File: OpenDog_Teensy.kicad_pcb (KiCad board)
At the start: 2 copper layers, 61.6 x 96 mm, 58 parts, among them J1 NRF, J10 UART5, J11 UART6, J12 CAN1, J13 CAN2, J14 EXP, J15 Power, J2 TOF1, J3 TOF2, J4 IMU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

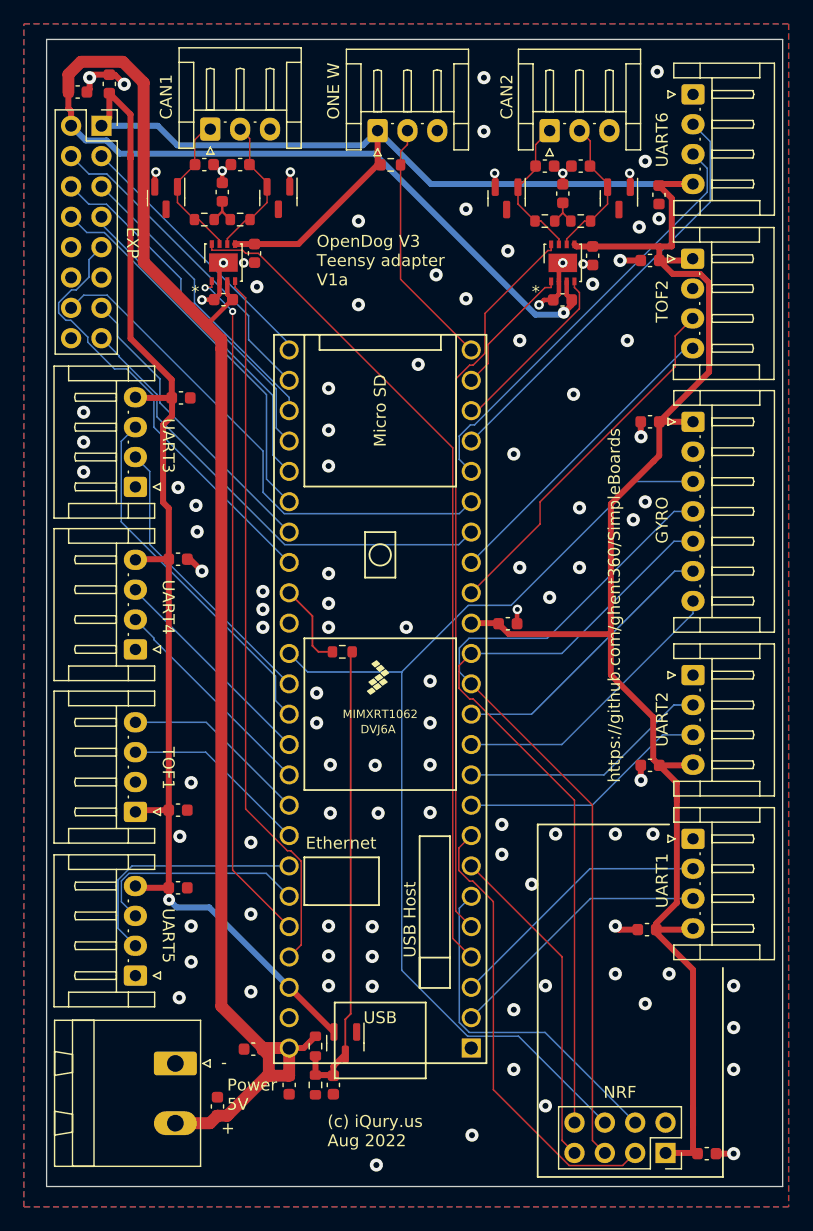
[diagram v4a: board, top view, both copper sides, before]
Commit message: Update OpenDog board part numbers. Small routing changes.
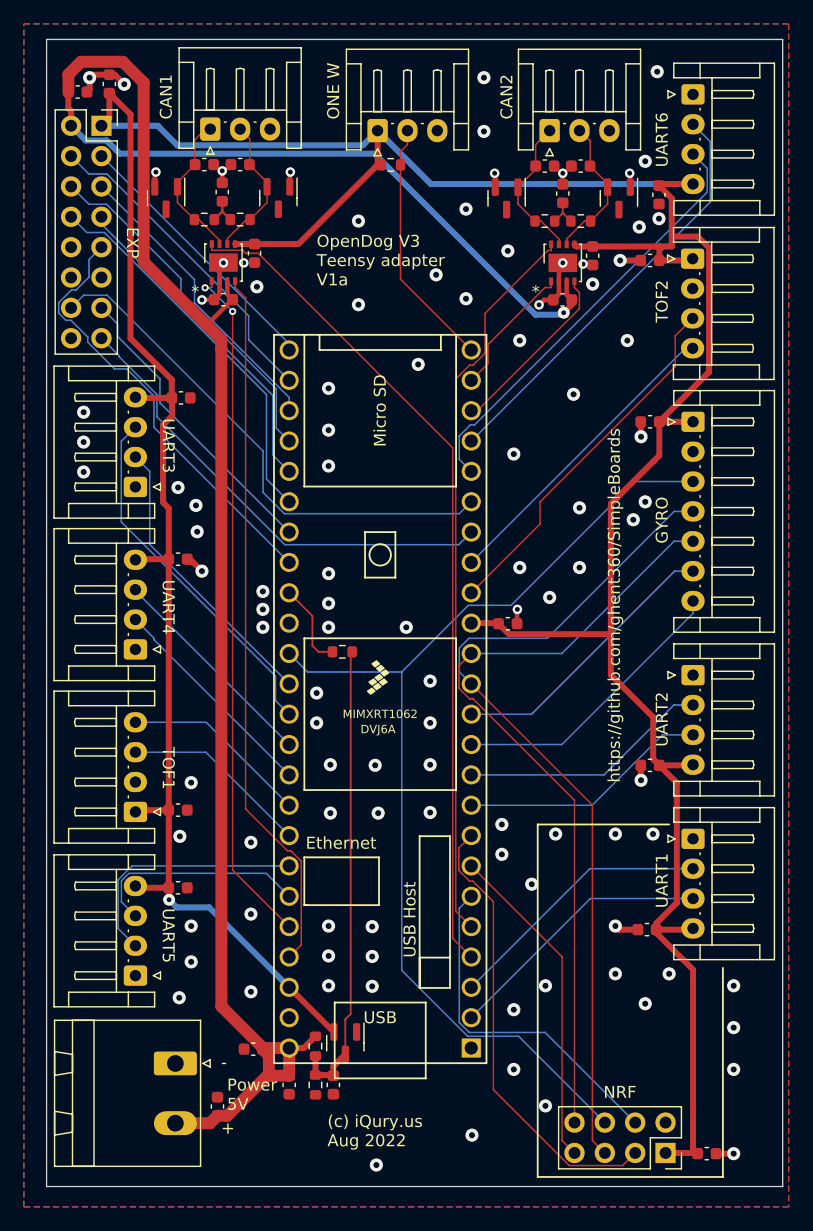
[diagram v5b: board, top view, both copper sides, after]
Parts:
- R1, R2, R3, R4: value 60 -> 60.4
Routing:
- net /3.3V: track 306.4 -> 305.0 mm
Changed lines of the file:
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@@
     (descr "Resistor SMD 0603 (1608 Metric), square (rectangular) end terminal, IPC_7351 nominal, (Body size source: IPC-SM-782 page 72, https://www.pcb-3d.com/wordpress/wp-content/uploads/ipc-sm-782a_amendment_1_and_2.pdf), generated with kicad-footprint-generator")
     (tags "resistor")
+    (property "JLC Part #" "C23090")
     (property "Sheetfile" "File: OpenDog_Teensy.kicad_sch")
     (property "Sheetname" "")
@@
         (effects (font (size 1 1) (thickness 0.15)))
     )
-    (fp_text value "60" (at 0 1.43) (layer "F.Fab")
+    (fp_text value "60.4" (at 0 1.43) (layer "F.Fab")
         (effects (font (size 1 1) (thickness 0.15)))
     )
@@
     (descr "Resistor SMD 0603 (1608 Metric), square (rectangular) end terminal, IPC_7351 nominal, (Body size source: IPC-SM-782 page 72, https://www.pcb-3d.com/wordpress/wp-content/uploads/ipc-sm-782a_amendment_1_and_2.pdf), generated with kicad-footprint-generator")
     (tags "resistor")
+    (property "JLC Part #" "C23090")
     (property "Sheetfile" "File: OpenDog_Teensy.kicad_sch")
     (property "Sheetname" "")
@@
         (effects (font (size 1 1) (thickness 0.15)))
     )
-    (fp_text value "60" (at 0 1.43) (layer "F.Fab")
+    (fp_text value "60.4" (at 0 1.43) (layer "F.Fab")
         (effects (font (size 1 1) (thickness 0.15)))
     )
@@
     (descr "Generic Phoenix Contact connector footprint for: MSTBA_2,5/2-G; number of pins: 02; pin pitch: 5.00mm; Angled || order number: 1757475 12A || order number: 1923759 16A (HC)")
     (tags "phoenix_contact connector MSTBA_01x02_G_5.00mm")
-    (property "JLC Part #" "C8439")
+    (property "JLC Part #" "C8404")
     (property "Sheetfile" "File: OpenDog_Teensy.kicad_sch")
     (property "Sheetname" "")
@@
     (descr "Resistor SMD 0603 (1608 Metric), square (rectangular) end terminal, IPC_7351 nominal, (Body size source: IPC-SM-782 page 72, https://www.pcb-3d.com/wordpress/wp-content/uploads/ipc-sm-782a_amendment_1_and_2.pdf), generated with kicad-footprint-generator")
     (tags "resistor")
+    (property "JLC Part #" "C23090")
     (property "Sheetfile" "File: OpenDog_Teensy.kicad_sch")
     (property "Sheetname" "")
@@
         (effects (font (size 1 1) (thickness 0.15)))
     )
-    (fp_text value "60" (at 0 1.43) (layer "F.Fab")
+    (fp_text value "60.4" (at 0 1.43) (layer "F.Fab")
         (effects (font (size 1 1) (thickness 0.15)))
     )
@@
     (descr "Resistor SMD 0603 (1608 Metric), square (rectangular) end terminal, IPC_7351 nominal, (Body size source: IPC-SM-782 page 72, https://www.pcb-3d.com/wordpress/wp-content/uploads/ipc-sm-782a_amendment_1_and_2.pdf), generated with kicad-footprint-generator")
     (tags "resistor")
+    (property "JLC Part #" "C23090")
     (property "Sheetfile" "File: OpenDog_Teensy.kicad_sch")
     (property "Sheetname" "")
@@
         (effects (font (size 1 1) (thickness 0.15)))
     )
-    (fp_text value "60" (at 0 1.43) (layer "F.Fab")
+    (fp_text value "60.4" (at 0 1.43) (layer "F.Fab")
         (effects (font (size 1 1) (thickness 0.15)))
     )
@@
   (segment (start 79.425 72.5) (end 78.923 72.5) (width 0.127) (layer "F.Cu") (net 8))
   (segment (start 79.375 67.9) (end 80.85 69.375) (width 0.127) (layer "F.Cu") (net 8))
-  (segment (start 40.923499 67.276501) (end 40.923499 66.958499) (width 0.5) (layer "F.Cu") (net 9))
+  (segment (start 86.225 70.6) (end 86.225 73.975) (width 0.5) (layer "F.Cu") (net 9))
+  (segment (start 86.4 73.8) (end 86.225 73.975) (width 0.5) (layer "F.Cu") (net 9))
   (segment (start 44.15 128.325) (end 44.125 128.3) (width 0.5) (layer "F.Cu") (net 9))
   (segment (start 85.225 74.625) (end 79.6 74.625) (width 0.5) (layer "F.Cu") (net 9))
-  (segment (start 88.60074 76.923) (end 89.3436 77.66586) (width 0.5) (layer "F.Cu") (net 9))
   (segment (start 81.1255 107.0707) (end 72.5957 107.0707) (width 0.5) (layer "F.Cu") (net 9))
   (segment (start 44.4 88.8) (end 44.4 87.325) (width 0.5) (layer "F.Cu") (net 9))
@@
   (segment (start 43.65 96.05) (end 43.65 89.55) (width 0.5) (layer "F.Cu") (net 9))
   (segment (start 40.923499 63.573499) (end 39.15 61.8) (width 0.5) (layer "F.Cu") (net 9))
-  (segment (start 85.175 75.8) (end 87.8175 75.8) (width 0.5) (layer "F.Cu") (net 9))
   (segment (start 44.125 128.3) (end 41.4825 128.3) (width 0.5) (layer "F.Cu") (net 9))
-  (segment (start 86.6466 120.5807) (end 86.6466 121.0534) (width 0.5) (layer "F.Cu") (net 9))
-  (segment (start 88 146.7) (end 88 148.19) (width 0.5) (layer "F.Cu") (net 9))
   (segment (start 44.375 85.775) (end 40.923499 82.323499) (width 0.5) (layer "F.Cu") (net 9))
   (segment (start 85.7 150.49) (end 88.315 150.49) (width 0.5) (layer "F.Cu") (net 9))
   (segment (start 44.125 100.8) (end 44.125 96.525) (width 0.5) (layer "F.Cu") (net 9))
   (segment (start 84.925 131.275) (end 84.925 131.8) (width 0.5) (layer "F.Cu") (net 9))
-  (segment (start 88 75.6175) (end 87.9675 75.65) (width 1) (layer "F.Cu") (net 9))
   (segment (start 84.6696 114.0304) (end 84.6696 117.5446) (width 0.5) (layer "F.Cu") (net 9))
   (segment (start 44.125 100.8) (end 41.3825 100.8) (width 0.5) (layer "F.Cu") (net 9))
@@
   (segment (start 41.4825 121.8) (end 41.3325 121.95) (width 0.5) (layer "F.Cu") (net 9))
   (segment (start 81.1255 96.1745) (end 81.1255 107.0707) (width 0.5) (layer "F.Cu") (net 9))
+  (segment (start 87.8175 75.8) (end 87.9675 75.65) (width 0.5) (layer "F.Cu") (net 9))
   (segment (start 85.275 69.4) (end 85.15 69.525) (width 0.5) (layer "F.Cu") (net 9))
   (segment (start 81.1255 110.4863) (end 84.6696 114.0304) (width 0.5) (layer "F.Cu") (net 9))
@@
   (segment (start 44.125 121.8) (end 44.125 100.8) (width 0.5) (layer "F.Cu") (net 9))
   (segment (start 85.15 69.525) (end 86.225 70.6) (width 0.5) (layer "F.Cu") (net 9))
+  (segment (start 86.225 73.975) (end 86.225 74.625) (width 0.5) (layer "F.Cu") (net 9))
   (segment (start 86.6466 121.0534) (end 86.6466 119.5216) (width 0.5) (layer "F.Cu") (net 9))
   (segment (start 88 135.15) (end 88 146.7) (width 0.5) (layer "F.Cu") (net 9))
   (segment (start 44.4 87.325) (end 44.375 87.3) (width 0.5) (layer "F.Cu") (net 9))
-  (segment (start 87.8175 75.8) (end 87.9675 75.65) (width 0.5) (layer "F.Cu") (net 9))
   (segment (start 51.3 74.425) (end 49.675 74.425) (width 0.5) (layer "F.Cu") (net 9))
+  (segment (start 89.3436 78.8564) (end 89.3436 74.7436) (width 0.5) (layer "F.Cu") (net 9))
+  (segment (start 85.175 75.8) (end 87.8175 75.8) (width 0.5) (layer "F.Cu") (net 9))
   (segment (start 88 150.175) (end 88.375 150.55) (width 0.5) (layer "F.Cu") (net 9))
   (segment (start 57.95 140.3625) (end 57.9325 140.3625) (width 0.5) (layer "F.Cu") (net 9))
-  (segment (start 86.298 76.923) (end 88.60074 76.923) (width 0.5) (layer "F.Cu") (net 9))
   (segment (start 44.125 121.8) (end 41.4825 121.8) (width 0.5) (layer "F.Cu") (net 9))
   (segment (start 85.175 89.3) (end 88 89.3) (width 0.5) (layer "F.Cu") (net 9))
   (segment (start 86.6466 119.5216) (end 85.175 118.05) (width 0.5) (layer "F.Cu") (net 9))
   (segment (start 89.3436 85.1314) (end 85.175 89.3) (width 0.5) (layer "F.Cu") (net 9))
+  (segment (start 89.3436 78.8564) (end 89.3436 85.1314) (width 0.5) (layer "F.Cu") (net 9))
   (segment (start 51.3 74.425) (end 54.975 74.425) (width 0.5) (layer "F.Cu") (net 9))
   (segment (start 39.15 61.8) (end 39.15 63.865) (width 0.5) (layer "F.Cu") (net 9))
@@
   (segment (start 86.6466 121.0534) (end 86.6466 129.5534) (width 0.5) (layer "F.Cu") (net 9))
   (segment (start 39.15 63.865) (end 38.49 64.525) (width 0.5) (layer "F.Cu") (net 9))
+  (segment (start 89.3436 74.7436) (end 88.4 73.8) (width 0.5) (layer "F.Cu") (net 9))
   (segment (start 57.9325 140.3625) (end 54.2 136.63) (width 0.5) (layer "F.Cu") (net 9))
   (segment (start 88 146.7) (end 88 150.175) (width 0.5) (layer "F.Cu") (net 9))
@@
   (segment (start 85.175 92.125) (end 85.175 89.3) (width 0.5) (layer "F.Cu") (net 9))
   (segment (start 54.975 74.425) (end 61.6 67.8) (width 0.5) (layer "F.Cu") (net 9))
-  (segment (start 86.225 70.6) (end 86.225 74.625) (width 0.5) (layer "F.Cu") (net 9))
   (segment (start 69.44 106.15) (end 71.675 106.15) (width 0.5) (layer "F.Cu") (net 9))
   (segment (start 85.175 74.675) (end 85.225 74.625) (width 0.5) (layer "F.Cu") (net 9))
   (segment (start 44.375 87.3) (end 41.3825 87.3) (width 0.5) (layer "F.Cu") (net 9))
   (segment (start 84.925 131.8) (end 84.925 132.075) (width 0.5) (layer "F.Cu") (net 9))
-  (segment (start 89.3436 77.66586) (end 89.3436 85.1314) (width 0.5) (layer "F.Cu") (net 9))
   (segment (start 44.375 87.3) (end 44.375 85.775) (width 0.5) (layer "F.Cu") (net 9))
   (segment (start 41.3825 87.3) (end 41.3325 87.25) (width 0.5) (layer "F.Cu") (net 9))
   (segment (start 87.9 131.8) (end 88 131.7) (width 0.5) (layer "F.Cu") (net 9))
-  (segment (start 88 117.3608) (end 88 118) (width 0.5) (layer "F.Cu") (net 9))
   (segment (start 61.6 67.8) (end 61.6 64.9325) (width 0.5) (layer "F.Cu") (net 9))
   (segment (start 85.175 75.8) (end 85.175 74.675) (width 0.5) (layer "F.Cu") (net 9))
+  (segment (start 88.4 73.8) (end 86.4 73.8) (width 0.5) (layer "F.Cu") (net 9))
   (segment (start 61.6 67.8) (end 61.875 67.8) (width 0.5) (layer "F.Cu") (net 9))
   (segment (start 84.6696 117.5446) (end 85.175 118.05) (width 0.5) (layer "F.Cu") (net 9))
   (segment (start 44.125 128.3) (end 44.125 121.8) (width 0.5) (layer "F.Cu") (net 9))
   (segment (start 85.175 118.05) (end 87.95 118.05) (width 0.5) (layer "F.Cu") (net 9))
-  (segment (start 85.175 75.8) (end 86.298 76.923) (width 0.5) (layer "F.Cu") (net 9))
   (via (at 44.15 129.3) (size 1) (drill 0.4) (layers "F.Cu" "B.Cu") (net 9))
   (segment (start 44.79 129.94) (end 44.15 129.3) (width 0.5) (layer "B.Cu") (net 9))

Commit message: Added I2C pullups to the OpenDog board.
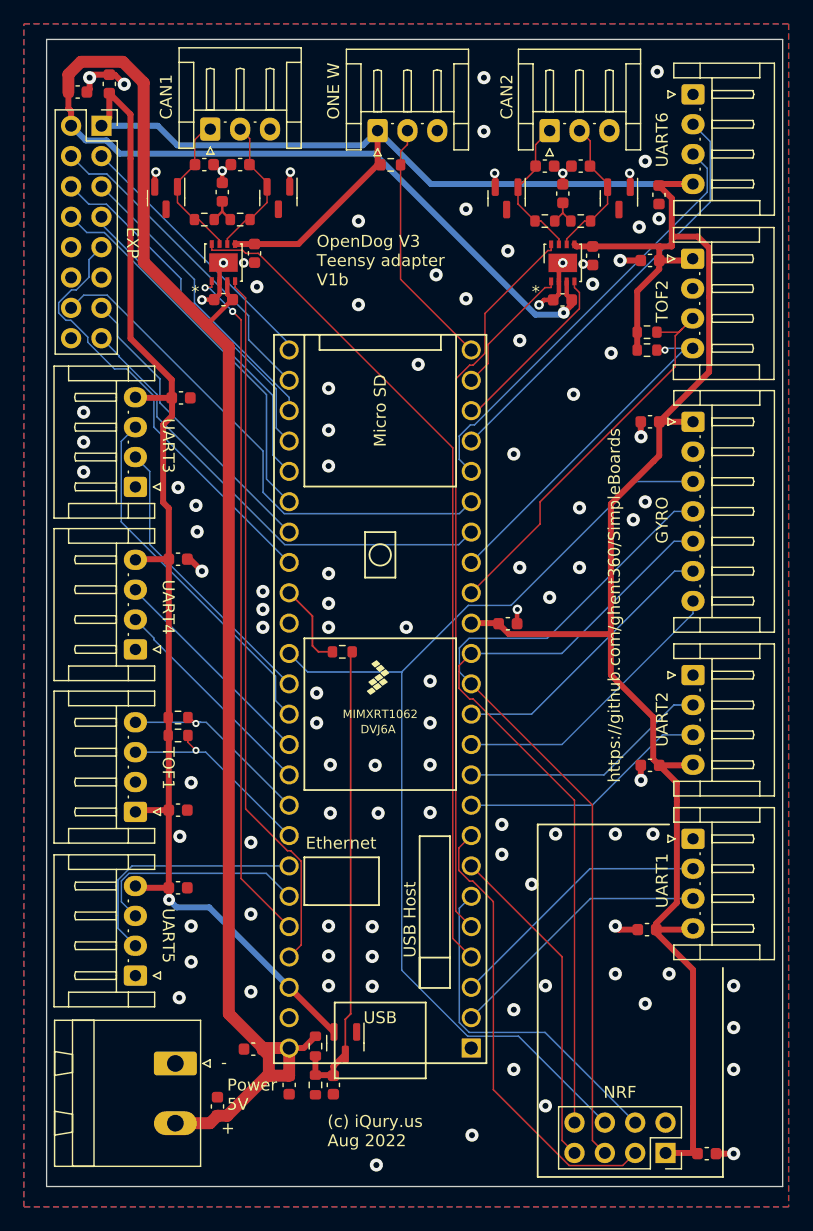
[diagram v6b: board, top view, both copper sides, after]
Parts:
- added R10: 1k, Resistor_SMD:R_0603_1608Metric, F.Cu at (44.9, 114.0)
- added R11: 1k, Resistor_SMD:R_0603_1608Metric, F.Cu at (84.2, 83.3)
- added R12: 1k, Resistor_SMD:R_0603_1608Metric, F.Cu at (84.2, 81.8)
- added R9: 1k, Resistor_SMD:R_0603_1608Metric, F.Cu at (44.9, 115.5)
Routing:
- net /3.3V: track 305.0 -> 313.3 mm
- net /SDA2: track 26.0 -> 29.0 mm, vias 0 -> 1
- net /SCL2: track 30.6 -> 32.9 mm
- net /SCL1: track 15.8 -> 17.5 mm, vias 0 -> 1
- net /SDA1: track 15.7 -> 17.1 mm, vias 0 -> 1
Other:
- board text added: "OpenDog V3 Teensy adapter V1b"
- board text removed: "OpenDog V3 Teensy adapter V1a"

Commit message: Fixed NRF connector pinout.
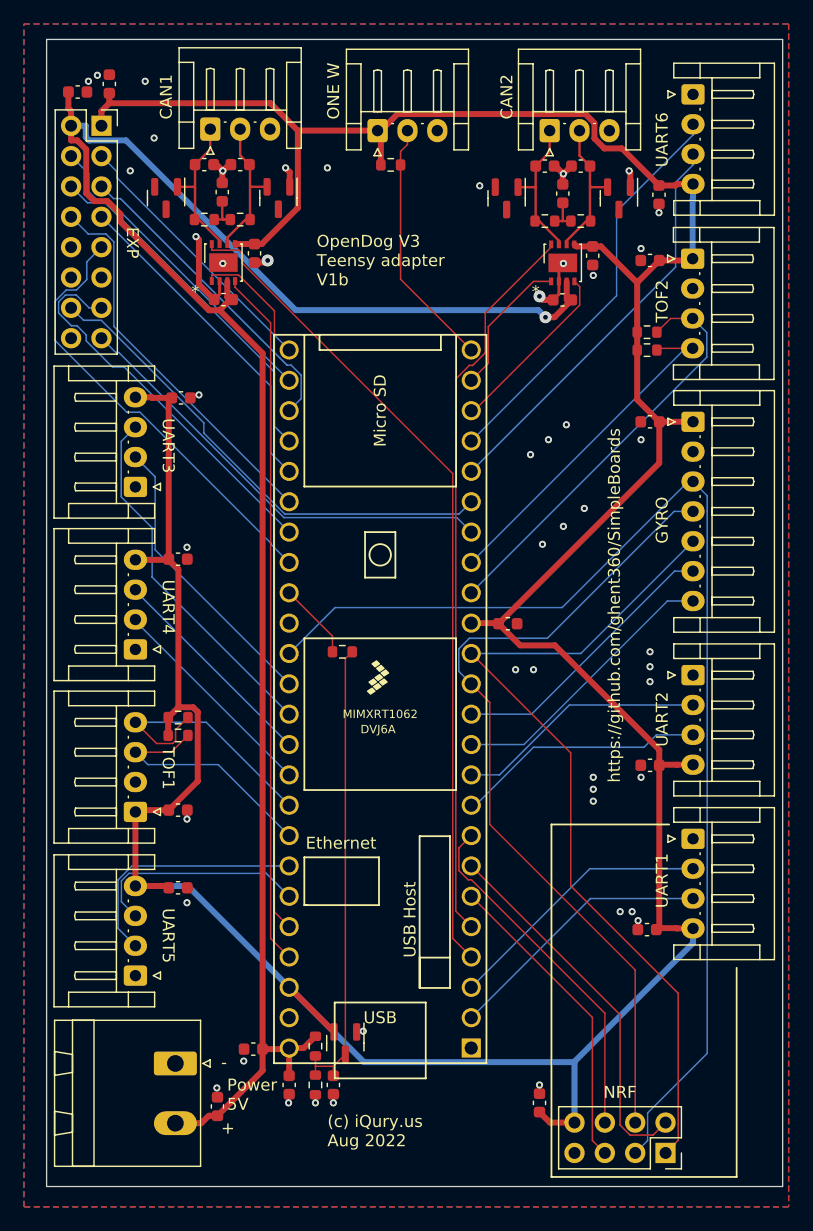
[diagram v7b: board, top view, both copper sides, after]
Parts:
- moved C24 14.6 mm to (75.2, 146.3), turned to 90 degrees
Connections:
- J1 pad 1: /3.3V -> /MISO
- J1 pad 2: GND -> /NRF_IRQ
- J1 pad 3: /~{CS_NRF} -> /SCK
- J1 pad 4: /NRF_ENA -> /MOSI
- J1 pad 5: /MOSI -> /NRF_ENA
- J1 pad 6: /SCK -> /~{CS_NRF}
- J1 pad 7: /NRF_IRQ -> GND
- J1 pad 8: /MISO -> /3.3V
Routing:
- net /3.3V: track 313.3 -> 299.0 mm, vias 1 -> 0
- net /VIn: track 173.6 -> 160.7 mm
- net /SCK: track 88.3 -> 98.9 mm
- net GND: track 31.2 -> 22.4 mm, vias 104 -> 49
- net /~{CS_NRF}: track 38.0 -> 29.7 mm
- net /MISO1: track 25.3 -> 32.4 mm
- net /MISO: track 66.3 -> 71.9 mm
- net /SDA1: track 17.1 -> 22.3 mm, vias 1 -> 0
- net /NRF_IRQ: track 27.6 -> 31.4 mm
- net /SCL1: track 17.5 -> 20.7 mm, vias 1 -> 0
- net /NRF_ENA: track 29.2 -> 26.1 mm
- net /SCK1: track 43.9 -> 41.6 mm
- net /SCL2: track 32.9 -> 35.1 mm
- net /RX6: track 36.3 -> 34.2 mm
- net /MOSI1: track 39.7 -> 37.7 mm
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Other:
- board text added: "IRQ MISO"
- board text added: "MOSI SCK"
- board text added: "~{CS} ENA"
- board text removed: "ENA CS"
- board text removed: "MISO IRQ"
- board text removed: "SCK MOSI"

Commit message: Add inverters to the opto serial adapter.
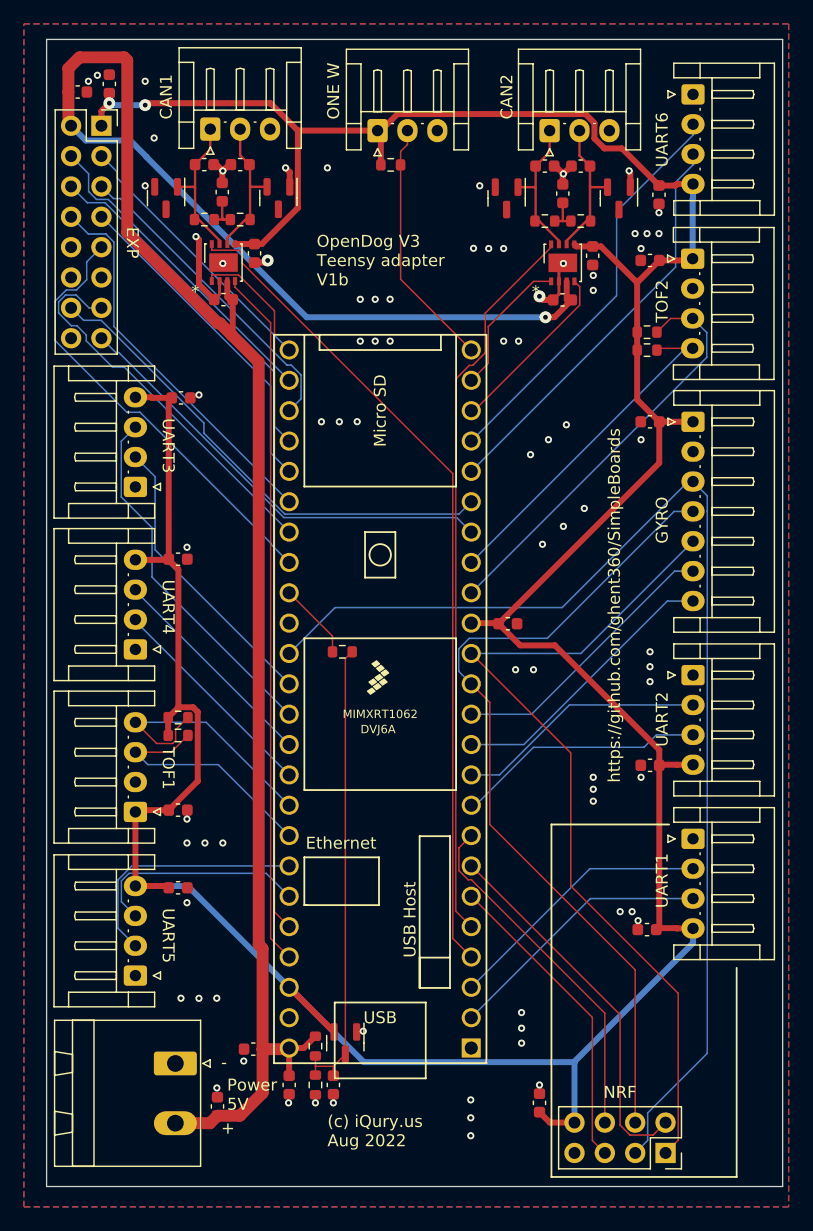
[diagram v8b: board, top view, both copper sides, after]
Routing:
- net /VIn: track 160.7 -> 172.7 mm
- net /3.3V: track 299.0 -> 299.2 mm, vias 0 -> 2
- net GND: vias 49 -> 79
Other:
- board text added: "CAN 2.0"
- board text added: "CAN FD"
